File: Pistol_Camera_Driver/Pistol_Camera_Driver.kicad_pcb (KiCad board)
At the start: 2 copper layers, 95.8 x 46.1 mm, 70 parts, among them J1 Screw_Terminal_01x02, J10 Bluetooth, J11 Screw_Terminal_01x02, J12 Screw_Terminal_01x02, J13 I2C, J14 Screw_Terminal_01x02, J15 Screw_Terminal_01x02, J2 Objective, J3 Screw_Terminal_01x02, J4 Screw_Terminal_01x02, J5 Screw_Terminal_01x02, J6 Joystick, J7 Screw_Terminal_01x02, J8 Screw_Terminal_01x02, J9 Screw_Terminal_01x02, K1 IM03, Q1 locked, U1 LM7805_TO220, U10 RS0101YH6, U11 LDD-700L, U12 RS0101YH6, U13 LDD-700L, U2 LM317_TO-263, U3 Raspberri_Pi_Pico, U4 DRV8834PWP, U5 DRV8834PWP, U6 RS0101YH6, U7 LDD-700L, U8 RS0101YH6, U9 LDD-700L

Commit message: v2.8 Full featured, DRC, ordered
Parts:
- J11: footprint Connector_PinSocket_2.54mm:PinSocket_1x02_P2.54mm_Vertical -> Connector_PinSocket_1.27mm:PinSocket_1x02_P1.27mm_Vertical
- moved J11 1.18 mm to (67.4, 40.4)
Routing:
- net Net-(D8-Pad2): track 40.4 -> 31.2 mm
- net +5V: track 160.1 -> 155.7 mm
- net +3.3VP: track 180.4 -> 178.2 mm
- net PWM_IR: track 42.3 -> 40.8 mm
- net +12V: track 114.6 -> 115.9 mm
- net Net-(J11-Pad2): track 6.84 -> 8.05 mm
- net Net-(J11-Pad1): track 6.56 -> 7.59 mm
- net SW: track 7.38 -> 7.96 mm
- net GND: vias 269 -> 307

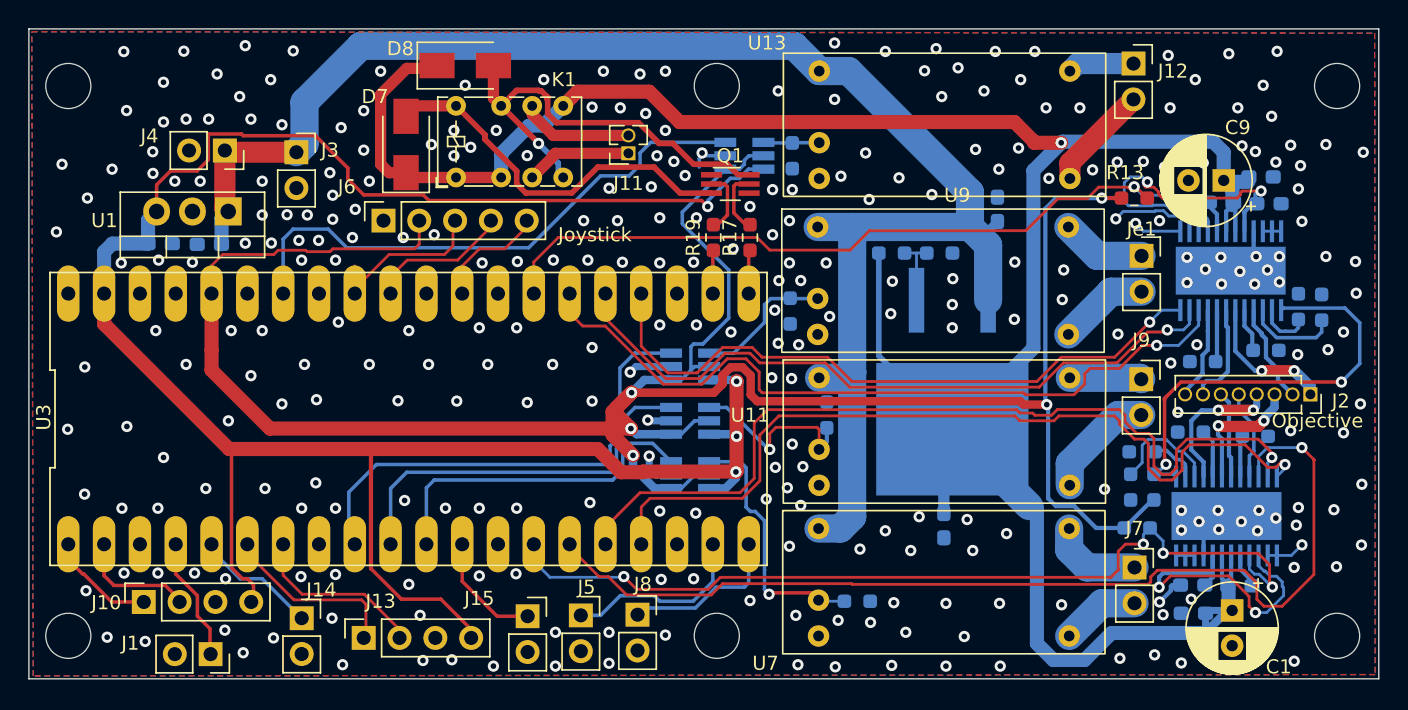
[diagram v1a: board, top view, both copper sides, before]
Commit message: v2.9 relay to 5 V, nMotorsSleep to RPI Pico
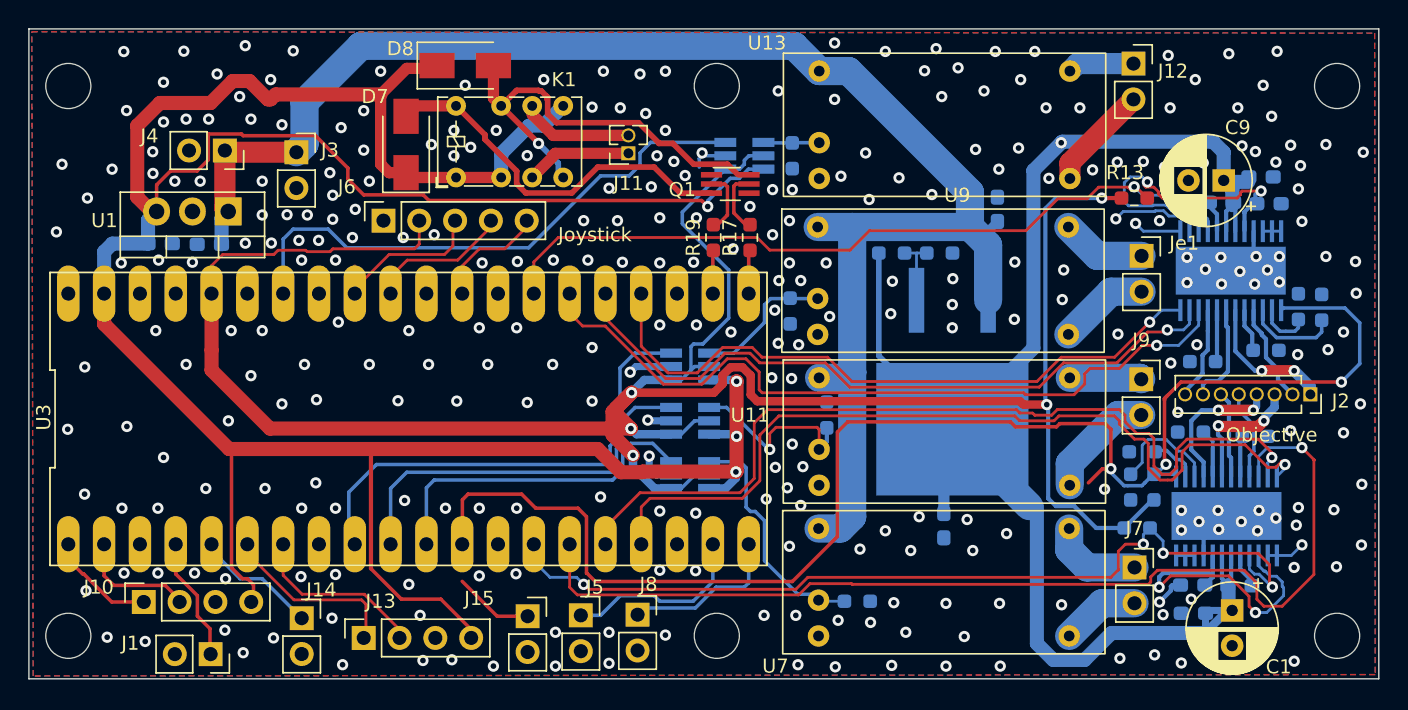
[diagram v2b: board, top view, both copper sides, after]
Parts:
- R10, R2, R4, R9: value R -> 470
- R11, R12, R5, R7: value R -> 3.9
- R16: value R -> 10 k
- R3: value R -> 240
- R6: value R -> 390
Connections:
- D7 pad 1: +3.3VP -> +5V
- D8 pad 1: +3.3VP -> +5V
- K1 pad 1: +3.3VP -> +5V
- K1 pad 2: +3.3VP -> +5V
- K1 pad 5: +3.3VP -> +5V
- U3 pad 12: K4 -> MOTORS_nSLEEP
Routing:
- net MOTORS_nSLEEP: track 31.9 -> 104.2 mm, vias 2 -> 3
- net +3.3VP: track 178.2 -> 114.8 mm
- net +5V: track 155.7 -> 207.9 mm
- net K4: track 8.30 -> 5.67 mm
- net nEN1: track 72.2 -> 73.8 mm
- net Net-(R14-Pad1): track 18.3 -> 17.0 mm, vias 1 -> 0
